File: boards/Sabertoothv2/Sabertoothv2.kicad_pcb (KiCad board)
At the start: 2 copper layers, 48.3 x 48.3 mm, 28 parts, among them J1 Screw_Terminal_01x04, J2 Screw_Terminal_01x04, J3 Conn_01x04_Pin, J4 Conn_01x04_Pin, Q1 NMOS, Q2 NMOS, Q3 NMOS, Q4 NMOS, U1 LM2104, U2 LM2104, U3 74LVC1GU04DRL

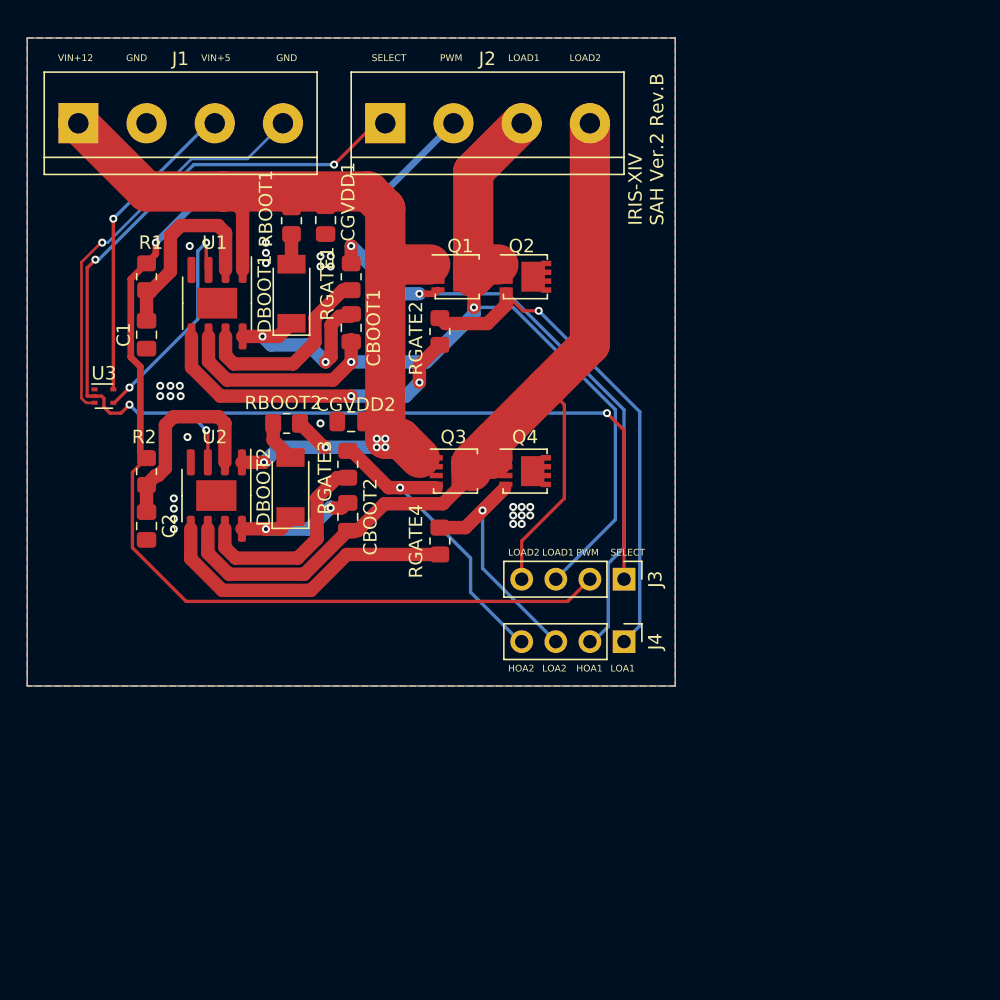
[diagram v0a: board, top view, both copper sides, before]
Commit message: added mount point
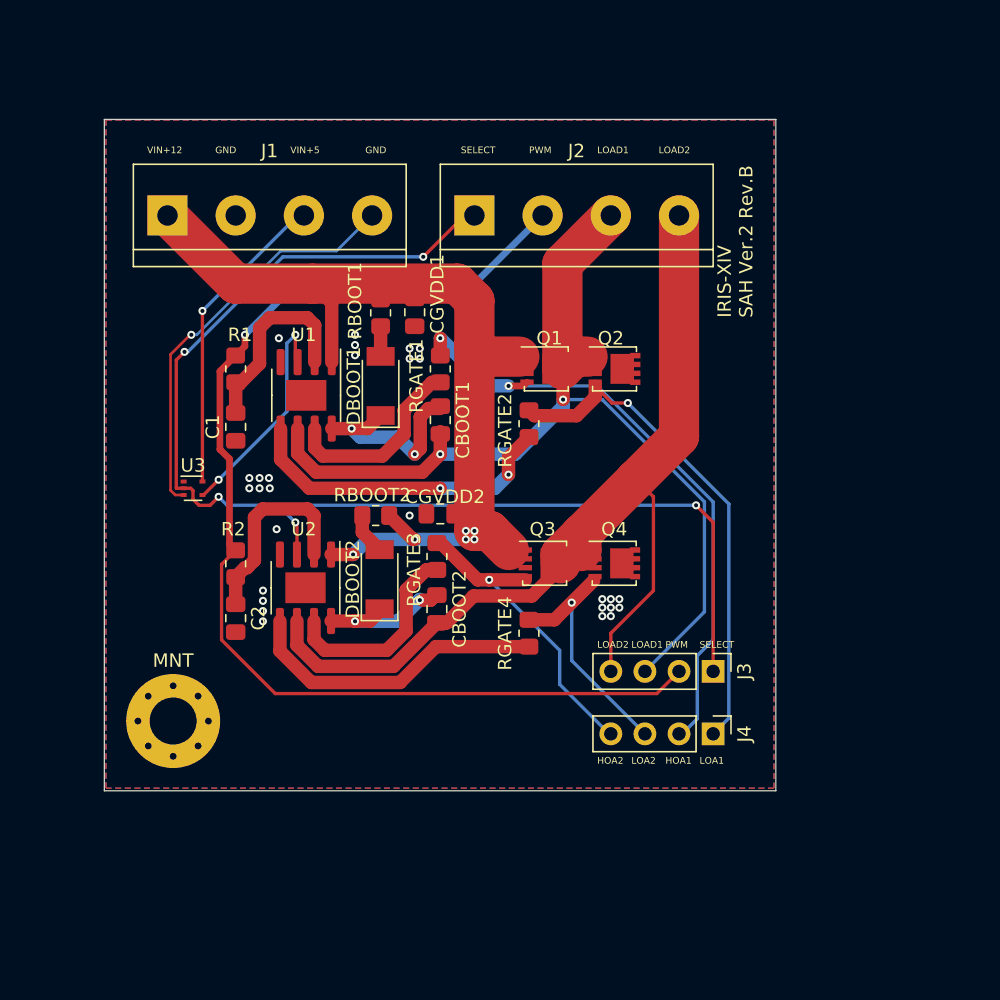
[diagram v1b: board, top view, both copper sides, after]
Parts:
- added MNT: MountingHole_3.5mm_Pad_Via, MountingHole:MountingHole_3.5mm_Pad_Via, F.Cu at (35.0, 75.0)
- moved G*** 9.55 mm to (73.9, 66.6)
- moved J4 9.55 mm to (75.2, 76.0)
- moved CBOOT1 9.55 mm to (54.9, 52.6)
- moved CBOOT2 9.55 mm to (54.6, 66.7)
- moved CGVDD2 9.55 mm to (54.9, 59.6)
- moved DBOOT1 9.55 mm to (50.5, 50.0)
- moved Q1 9.55 mm to (63.2, 48.8)
- moved Q2 9.55 mm to (68.2, 48.8)
- moved Q3 9.55 mm to (63.0, 63.3)
- moved Q4 9.55 mm to (68.2, 63.3)
- moved RBOOT1 9.55 mm to (50.5, 44.6)
- moved RGATE1 9.55 mm to (54.9, 48.8)
- moved U2 9.55 mm to (44.9, 65.1)
- moved U3 9.55 mm to (36.5, 57.7)
- moved J2 9.55 mm to (57.4, 37.3)
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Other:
- board size 48.3 x 48.3 mm -> 50 x 50 mm

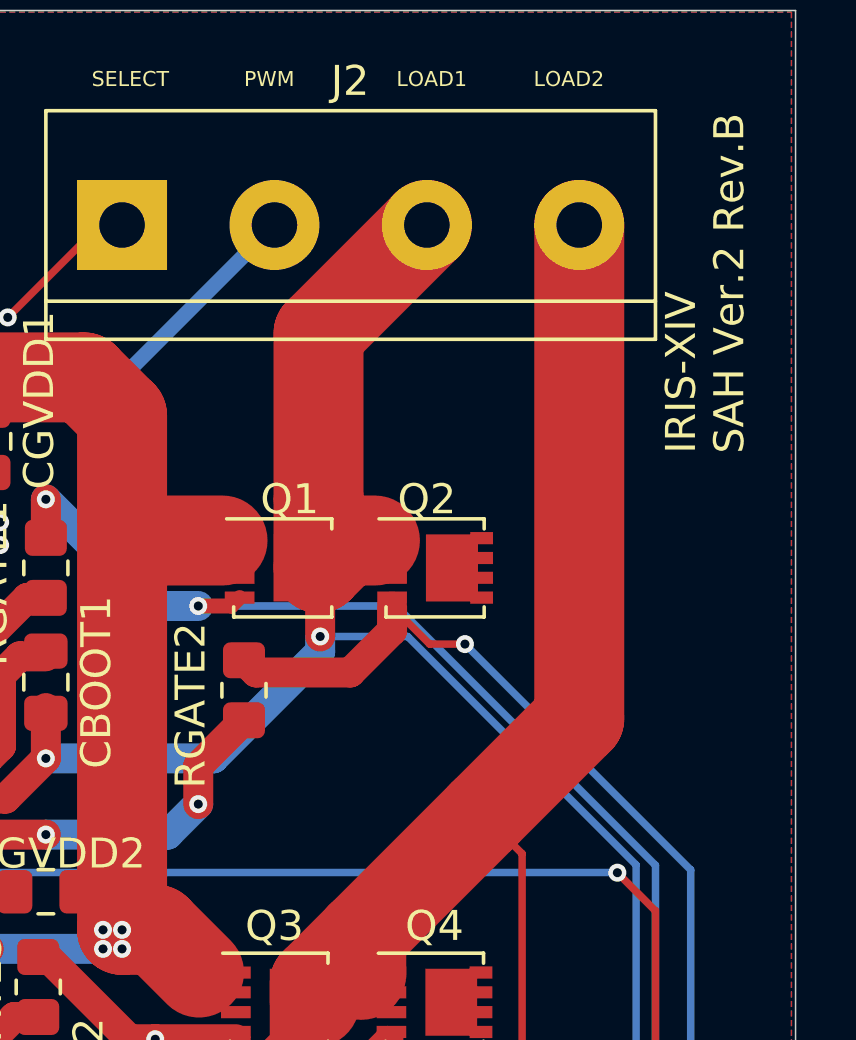
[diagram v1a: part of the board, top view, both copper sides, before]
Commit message: added spaces inbetween loads so we can add capacitors or other stuff so hopefully board works better
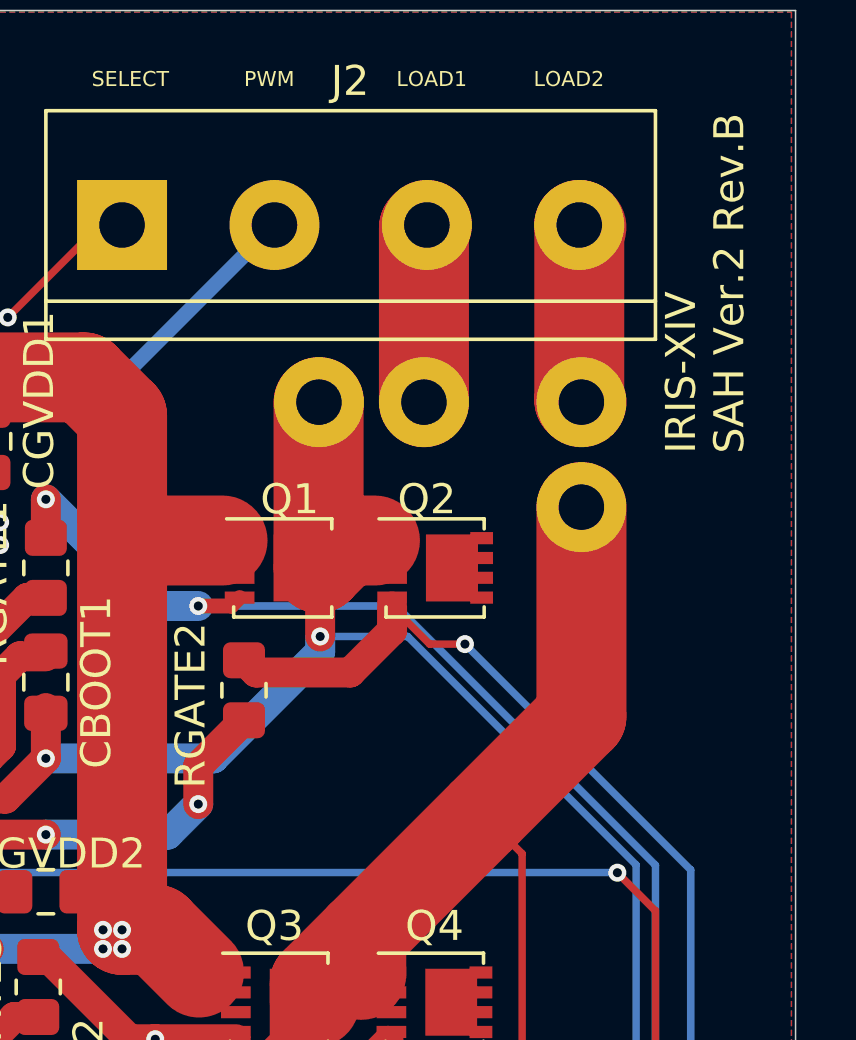
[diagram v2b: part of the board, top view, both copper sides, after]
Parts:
- added ?: , , F.Cu at (72.8, 46.8)
- added ?: , , F.Cu at (64.0, 43.2)
- added ?: , , F.Cu at (67.5, 43.2)
- added ?: , , F.Cu at (72.8, 43.2)
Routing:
- net LOAD2: track 72.2 -> 68.8 mm
- net LOAD1: track 72.1 -> 70.6 mm
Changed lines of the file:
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@@
       (disableapertmacros false)
       (usegerberextensions true)
-      (usegerberattributes true)
+      (usegerberattributes false)
       (usegerberadvancedattributes false)
-      (creategerberjobfile true)
+      (creategerberjobfile false)
       (dashed_line_dash_ratio 12.000000)
       (dashed_line_gap_ratio 3.000000)
@@
     )
   )
+  (footprint "" (layer "F.Cu")
+    (at 72.75 46.75)
+    (fp_text reference "" (at 0 0) (layer "F.SilkS")
+        (effects (font (size 1.27 1.27) (thickness 0.15)))
+    )
+    (fp_text value "" (at 0 0) (layer "F.SilkS")
+        (effects (font (size 1.27 1.27) (thickness 0.15)))
+    )
+    (pad "LOAD2_TEST1" thru_hole circle (at 0 0) (size 3 3) (drill 1.52) (layers "*.Cu" "*.Mask")
+      (net 11 "LOAD2") (pinfunction "Pin_4") (pintype "passive"))
+  )
   (footprint "Resistor_SMD:R_0805_2012Metric_Pad1.20x1.40mm_HandSolder" (layer "F.Cu")
     (at 61.501157 68.46 90)
@@
     )
   )
+  (footprint "" (layer "F.Cu")
+    (at 64 43.25)
+    (fp_text reference "" (at 0 0) (layer "F.SilkS")
+        (effects (font (size 1.27 1.27) (thickness 0.15)))
+    )
+    (fp_text value "" (at 0 0) (layer "F.SilkS")
+        (effects (font (size 1.27 1.27) (thickness 0.15)))
+    )
+    (pad "LOAD1_TEST1" thru_hole circle (at 0 0) (size 3 3) (drill 1.52) (layers "*.Cu" "*.Mask")
+      (net 10 "LOAD1") (pinfunction "Pin_3") (pintype "passive"))
+  )
   (footprint "TerminalBlock:TerminalBlock_bornier-4_P5.08mm" (layer "F.Cu")
     (at 34.577157 37.345)
@@
     )
   )
+  (footprint "" (layer "F.Cu")
+    (at 67.5 43.25)
+    (fp_text reference "" (at 0 0) (layer "F.SilkS")
+        (effects (font (size 1.27 1.27) (thickness 0.15)))
+    )
+    (fp_text value "" (at 0 0) (layer "F.SilkS")
+        (effects (font (size 1.27 1.27) (thickness 0.15)))
+    )
+    (pad "LOAD1_TEST2" thru_hole circle (at 0 0) (size 3 3) (drill 1.52) (layers "*.Cu" "*.Mask")
+      (net 10 "LOAD1") (pinfunction "Pin_3") (pintype "passive"))
+  )
   (footprint "mosfet:PPAK1212-8Custom" (layer "F.Cu")
     (at 63.152157 48.775)
@@
       ))
   )
+  (footprint "" (layer "F.Cu")
+    (at 72.75 43.25)
+    (fp_text reference "" (at 0 0) (layer "F.SilkS")
+        (effects (font (size 1.27 1.27) (thickness 0.15)))
+    )
+    (fp_text value "" (at 0 0) (layer "F.SilkS")
+        (effects (font (size 1.27 1.27) (thickness 0.15)))
+    )
+    (pad "LOAD2_TEST2" thru_hole circle (at 0 0) (size 3 3) (drill 1.52) (layers "*.Cu" "*.Mask")
+      (net 11 "LOAD2") (pinfunction "Pin_4") (pintype "passive"))
+  )
   (footprint "mosfet:PPAK1212-8Custom" (layer "F.Cu")
     (at 68.211157 63.253)
@@
   (segment (start 45.650101 56.465) (end 53.557157 56.465) (width 1) (layer "F.Cu") (net 10))
   (segment (start 44.272157 55.087056) (end 45.650101 56.465) (width 1) (layer "F.Cu") (net 10))
-  (segment (start 63.987157 40.955) (end 63.987157 46.489) (width 3) (layer "F.Cu") (net 10))
+  (segment (start 64 43.25) (end 63.987157 43.262843) (width 3) (layer "F.Cu") (net 10))
+  (segment (start 63.987157 43.262843) (end 63.987157 48.775) (width 3) (layer "F.Cu") (net 10))
+  (segment (start 67.5 43.25) (end 67.5 37.442157) (width 3) (layer "F.Cu") (net 10))
   (segment (start 63.987157 48.775) (end 64.899657 47.8625) (width 3) (layer "F.Cu") (net 10))
   (segment (start 64.041157 48.829) (end 63.987157 48.775) (width 1) (layer "F.Cu") (net 10))
   (segment (start 44.272157 53.22) (end 44.272157 55.087056) (width 1) (layer "F.Cu") (net 10))
-  (segment (start 67.597157 37.345) (end 63.987157 40.955) (width 3) (layer "F.Cu") (net 10))
   (segment (start 54.897157 55.125) (end 54.897157 53.4475) (width 1) (layer "F.Cu") (net 10))
   (segment (start 53.557157 56.465) (end 54.897157 55.125) (width 1) (layer "F.Cu") (net 10))
   (segment (start 64.041157 51.061) (end 64.041157 48.829) (width 1) (layer "F.Cu") (net 10))
-  (segment (start 63.987157 46.489) (end 63.987157 48.775) (width 3) (layer "F.Cu") (net 10))
+  (segment (start 67.5 37.442157) (end 67.597157 37.345) (width 3) (layer "F.Cu") (net 10))
   (segment (start 64.899657 47.8625) (end 65.867157 47.8625) (width 3) (layer "F.Cu") (net 10))
   (via (at 54.897157 55.125) (size 0.6) (drill 0.3) (layers "F.Cu" "B.Cu") (net 10))
@@
   (segment (start 44.222157 69.358583) (end 45.793574 70.93) (width 1) (layer "F.Cu") (net 11))
   (segment (start 54.643157 67.693) (end 55.368157 67.693) (width 1) (layer "F.Cu") (net 11))
+  (segment (start 72.75 46.75) (end 72.75 53.725657) (width 3) (layer "F.Cu") (net 11))
+  (segment (start 72.677157 43.177157) (end 72.75 43.25) (width 3) (layer "F.Cu") (net 11))
   (segment (start 61.727213 65.6855) (end 63.222657 64.190056) (width 1) (layer "F.Cu") (net 11))
   (segment (start 44.222157 67.55) (end 44.222157 69.358583) (width 1) (layer "F.Cu") (net 11))
   (segment (start 65.409907 61.06575) (end 63.860157 62.6155) (width 3) (layer "F.Cu") (net 11))
   (segment (start 57.375657 65.6855) (end 61.727213 65.6855) (width 1) (layer "F.Cu") (net 11))
+  (segment (start 72.677157 37.345) (end 72.677157 43.177157) (width 3) (layer "F.Cu") (net 11))
   (segment (start 70.772157 65.285) (end 70.772157 58.3) (width 0.25) (layer "F.Cu") (net 11))
   (segment (start 70.772157 58.3) (end 69.473907 57.00175) (width 0.25) (layer "F.Cu") (net 11))
-  (segment (start 72.677157 37.345) (end 72.677157 53.7985) (width 3) (layer "F.Cu") (net 11))
   (segment (start 67.597157 68.46) (end 70.772157 65.285) (width 0.25) (layer "F.Cu") (net 11))
   (segment (start 51.406157 70.93) (end 54.643157 67.693) (width 1) (layer "F.Cu") (net 11))
@@
   (segment (start 55.368157 67.693) (end 57.375657 65.6855) (width 1) (layer "F.Cu") (net 11))
   (segment (start 63.860157 62.6155) (end 63.860157 63.253) (width 3) (layer "F.Cu") (net 11))
-  (segment (start 72.677157 53.7985) (end 69.473907 57.00175) (width 3) (layer "F.Cu") (net 11))
+  (segment (start 72.75 53.725657) (end 69.473907 57.00175) (width 3) (layer "F.Cu") (net 11))
   (segment (start 45.793574 70.93) (end 51.406157 70.93) (width 1) (layer "F.Cu") (net 11))
   (segment (start 65.409907 61.06575) (end 65.409907 62.3405) (width 3) (layer "F.Cu") (net 11))
+  (segment (start 72.75 37.417843) (end 72.677157 37.345) (width 3) (layer "F.Cu") (net 11))
   (segment (start 35.257157 57.665) (end 35.782157 57.665) (width 0.25) (layer "F.Cu") (net 12))
   (segment (start 36.482157 58.49) (end 36.927157 58.935) (width 0.25) (layer "F.Cu") (net 12))

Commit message: new schematic idea
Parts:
- removed ? (x4): , 
- C1, C2, CBOOT1, CBOOT2, CGVDD1, CGVDD2: footprint Capacitor_SMD:C_0805_2012Metric_Pad1.18x1.45mm_HandSolder -> Capacitor_SMD:C_0805_2012Metric
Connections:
- net HOA1 renamed HOA
- net HOA2 renamed HOB
- net LOA1 renamed LOA
- net LOA2 renamed LOB
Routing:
- net LOAD2: track 68.8 -> 72.2 mm
- net LOAD1: track 70.6 -> 72.1 mm

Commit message: changing pcb
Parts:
- added ANTIPARALLEL1: 1V, Diode_SMD:D_SOD-128, F.Cu at (52.5, 48.5)
- added ANTIPARALLEL2: 1V, Diode_SMD:D_SOD-128, F.Cu at (58.5, 48.5)
- added ANTIPARALLEL3: 1V, Diode_SMD:D_SOD-128, F.Cu at (86.3, 51.0)
- added ANTIPARALLEL4: 1V, Diode_SMD:D_SOD-128, F.Cu at (86.3, 55.0)
- added Q5: NMOS, mosfet:PPAK1212-8Custom, F.Cu at (34.5, 46.5)
- added Q6: NMOS, mosfet:PPAK1212-8Custom, F.Cu at (93.0, 47.7)
- moved U2 47.3 mm to (90.8, 76.6)
- moved RGATE3 30.0 mm to (69.7, 88.7)
- moved DBOOT2 30.0 mm to (65.5, 90.4)
- moved Q4 30.0 mm to (83.3, 89.2)
- moved R2 30.0 mm to (54.7, 89.2)
- moved Q3 30.0 mm to (78.1, 89.2)
- moved RGATE4 29.5 mm to (86.4, 84.3)
- moved C2 29.5 mm to (64.5, 83.2)
- moved CBOOT2 29.5 mm to (79.5, 82.5)
- moved CGVDD2 18.9 mm to (73.7, 61.6)
- moved RBOOT2 14.0 mm to (59.0, 70.5)
- moved Q2 7.63 mm to (75.8, 47.8)
- moved U3 7.43 mm to (33.2, 51.0)
- moved RGATE2 7.13 mm to (55.5, 49.0)
- moved CBOOT1 5.97 mm to (49.0, 53.5)
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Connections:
- J4 pad 1: LOA -> VIN+12
- J4 pad 2: HOA -> GND
- J4 pad 3: LOB -> LOA
- J4 pad 4: HOB -> HOA
- R1 pad 1: PWM -> Net-(Q5-S)
- R2 pad 1: PWM -> Net-(Q6-S)
- U1 pad 3: Net-(U1-SD') -> VIN+5
- U2 pad 3: SELECT -> VIN+5
- U3 pad 3: LGND -> GND
- U3 pad 4: Net-(U1-SD') -> Net-(Q5-G)
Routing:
- net LOAD2: track 72.2 -> 0.00 mm
- net PWM: track 86.7 -> 34.4 mm
- net SELECT: track 93.5 -> 44.3 mm, vias 5 -> 0
- net LOAD1: track 72.1 -> 29.6 mm, vias 2 -> 0
- net LOA: track 37.7 -> 0.00 mm, vias 1 -> 0
- net LGND: track 30.5 -> 0.00 mm, vias 1 -> 0
- net HOA: track 46.6 -> 20.0 mm
- net Net-(ANTIPARALLEL2-A): track 24.0 -> 0.00 mm, vias 2 -> 0
- net HOB: track 23.0 -> 0.00 mm, vias 1 -> 0
- net Net-(ANTIPARALLEL4-A): track 22.9 -> 0.00 mm
- net LOB: track 18.1 -> 0.00 mm, vias 1 -> 0
- net VIN+12: track 71.6 -> 54.0 mm, vias 6 -> 0
- net Net-(U1-SD'): track 16.9 -> 0.00 mm, vias 2 -> 0
- net Net-(ANTIPARALLEL3-A): track 15.1 -> 0.00 mm
- net Net-(U2-IN): track 15.0 -> 0.00 mm
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- removed copper zone on B.Cu, net GND
- removed copper zone on F.Cu, net GND

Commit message: almsot done
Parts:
- removed MNT: MountingHole_3.5mm_Pad_Via, MountingHole:MountingHole_3.5mm_Pad_Via
- Q1, Q2, Q3, Q4: footprint mosfet:PPAK1212-8Custom -> Package_TO_SOT_THT:TO-220-3_Vertical
- moved Q6 60.8 mm to (34.2, 63.2)
- moved U2 50.6 mm to (41.2, 66.7)
- moved ANTIPARALLEL3 37.1 mm to (53.0, 67.2), turned to 90 degrees
- moved RGATE4 34.4 mm to (56.2, 67.8)
- moved CBOOT2 31.8 mm to (49.5, 72.0)
- moved ANTIPARALLEL4 29.9 mm to (59.0, 67.2), turned to 90 degrees
- moved Q4 29.8 mm to (76.0, 60.2), turned to -90 degrees
- moved C2 29.8 mm to (36.5, 73.0)
- moved RGATE3 29.5 mm to (49.5, 67.2)
- moved DBOOT2 28.6 mm to (46.5, 69.0)
- moved R2 27.6 mm to (36.5, 68.5)
- moved Q3 26.0 mm to (68.4, 65.0), turned to 90 degrees
- moved CGVDD2 24.2 mm to (49.5, 62.7), turned to -90 degrees
- moved RBOOT2 14.8 mm to (46.5, 62.5), turned to -90 degrees
- moved Q2 2.88 mm to (76.1, 45.0), turned to -90 degrees
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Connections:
- ANTIPARALLEL1 pad 1: HOA -> Net-(ANTIPARALLEL1-K)
- ANTIPARALLEL1 pad 2: Net-(ANTIPARALLEL1-A) -> HOA
- ANTIPARALLEL2 pad 1: LOA -> Net-(ANTIPARALLEL2-K)
- ANTIPARALLEL2 pad 2: Net-(ANTIPARALLEL2-A) -> LOA
- ANTIPARALLEL3 pad 1: HOB -> Net-(ANTIPARALLEL3-K)
- ANTIPARALLEL3 pad 2: Net-(ANTIPARALLEL3-A) -> HOB
- ANTIPARALLEL4 pad 1: LOB -> Net-(ANTIPARALLEL4-K)
- ANTIPARALLEL4 pad 2: Net-(ANTIPARALLEL4-A) -> LOB
- J1 pad 1: VIN+12 -> SELECT
- J1 pad 2: GND -> PWM
- J2 pad 1: SELECT -> VIN+12
- J2 pad 2: PWM -> GND
- RGATE1 pad 1: Net-(ANTIPARALLEL1-A) -> Net-(ANTIPARALLEL1-K)
- RGATE2 pad 1: Net-(ANTIPARALLEL2-A) -> Net-(ANTIPARALLEL2-K)
- RGATE3 pad 1: Net-(ANTIPARALLEL3-A) -> Net-(ANTIPARALLEL3-K)
- RGATE4 pad 1: Net-(ANTIPARALLEL4-A) -> Net-(ANTIPARALLEL4-K)
- U1 pad 5: Net-(ANTIPARALLEL2-A) -> Net-(ANTIPARALLEL2-K)
- U1 pad 7: Net-(ANTIPARALLEL1-A) -> Net-(ANTIPARALLEL1-K)
- U2 pad 5: Net-(ANTIPARALLEL4-A) -> Net-(ANTIPARALLEL4-K)
- U2 pad 7: Net-(ANTIPARALLEL3-A) -> Net-(ANTIPARALLEL3-K)
- U3 pad 3: GND -> LGND
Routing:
- net LOAD2: track 0.00 -> 59.3 mm
- net LGND: track 0.00 -> 36.2 mm
- net LOA: track 0.00 -> 31.6 mm, vias 0 -> 2
- net LOAD1: track 29.6 -> 60.6 mm, vias 0 -> 2
- net Net-(ANTIPARALLEL2-K): track 0.00 -> 27.3 mm
- net Net-(ANTIPARALLEL4-K): track 0.00 -> 27.3 mm
- net VIN+12: track 54.0 -> 78.1 mm
- net VIN+5: track 33.9 -> 53.7 mm, vias 2 -> 3
- net Net-(ANTIPARALLEL1-K): track 0.00 -> 17.1 mm, vias 0 -> 2
- net Net-(ANTIPARALLEL1-A): track 16.7 -> 0.00 mm, vias 2 -> 0
- net Net-(ANTIPARALLEL3-K): track 0.00 -> 15.6 mm, vias 0 -> 2
- net Net-(U2-IN): track 0.00 -> 15.0 mm, vias 0 -> 2
- net SELECT: track 44.3 -> 31.2 mm
- net Net-(DBOOT2-K): track 0.00 -> 7.31 mm
- net Net-(Q6-S): track 0.00 -> 5.15 mm
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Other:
- board text added: "LGND"
